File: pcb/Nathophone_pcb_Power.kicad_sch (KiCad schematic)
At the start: 54 parts, among them J1 PJ-063AH, J12 54202-S0806ALF, Q1 2N7002H, Q2 2N7002H, Q3 FDN340P, Q4 FQD11P06TM, Q5 FDN340P, SW1 1-1571986-1, U1 LT8650SEV_PBF, U2 SPX3819M5-L-3-3

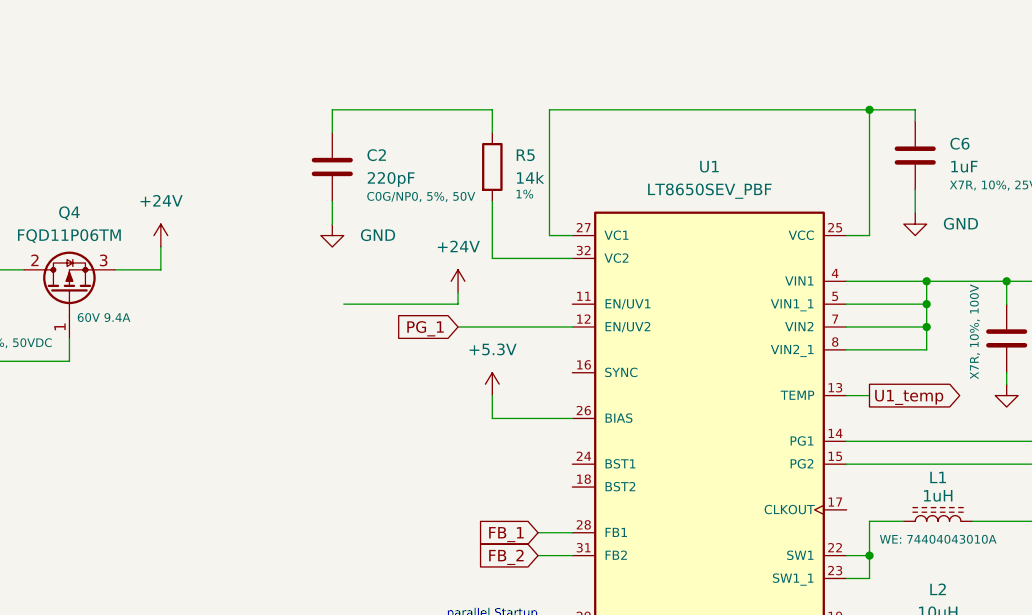
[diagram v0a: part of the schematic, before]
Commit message: ADDED Grounding Structure
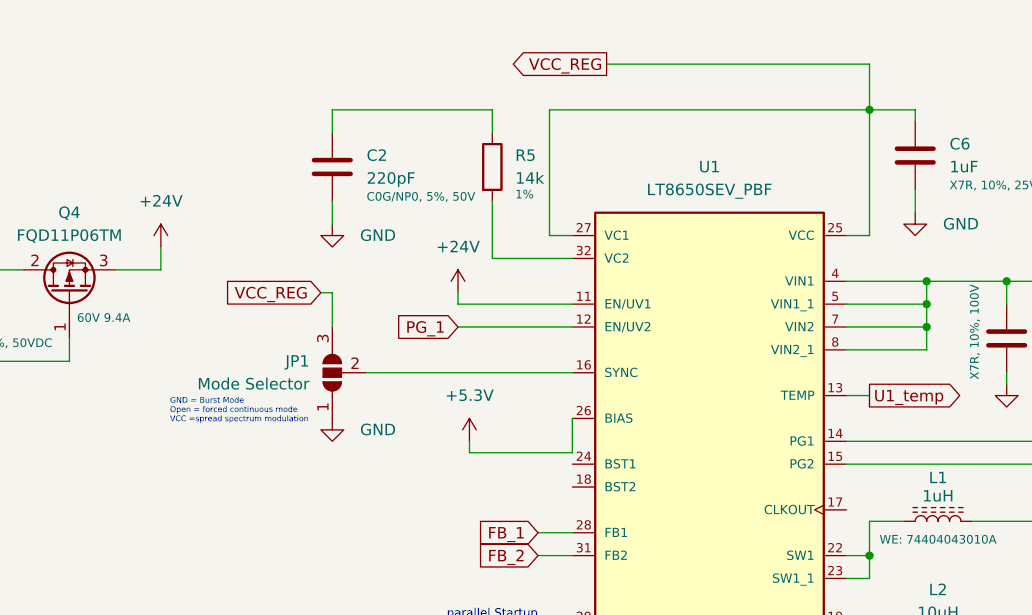
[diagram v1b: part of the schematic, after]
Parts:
- added JP1: Mode Selector, Jumper:SolderJumper-3_P1.3mm_Open_RoundedPad1.0x1.5mm, symbol Jumper:SolderJumper_3_Open
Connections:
- net +24V: now also U1.11 (EN/UV1)
- net GND: now also JP1.1 (A)
- net VCC_REG: now reaches C6.1, U1.25 (VCC), U1.27 (VC1)
- net VCC_REG: now also JP1.3 (B)
- net at U1.16 (SYNC): now also JP1.2 (C)
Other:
- note added: "GND = Burst Mode Open = forced continuous mode VCC =spread spectrum modulation"

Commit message: FINISHED Version 1, Checked heights
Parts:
- added F5, F6, F7: Polyfuse, Fuse:Fuse_1206_3216Metric, symbol Device:Polyfuse
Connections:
- net +24V: now also F6.1; no longer J12.2 (Pin_2)
- net +3.3V_int: now also F7.1; no longer J12.6 (Pin_6)
- net +5.3V: now also F5.1; no longer J12.4 (Pin_4)
- new net: F5.2, J12.4 (Pin_4)
- new net: F6.2, J12.2 (Pin_2)
- new net: F7.2, J12.6 (Pin_6)

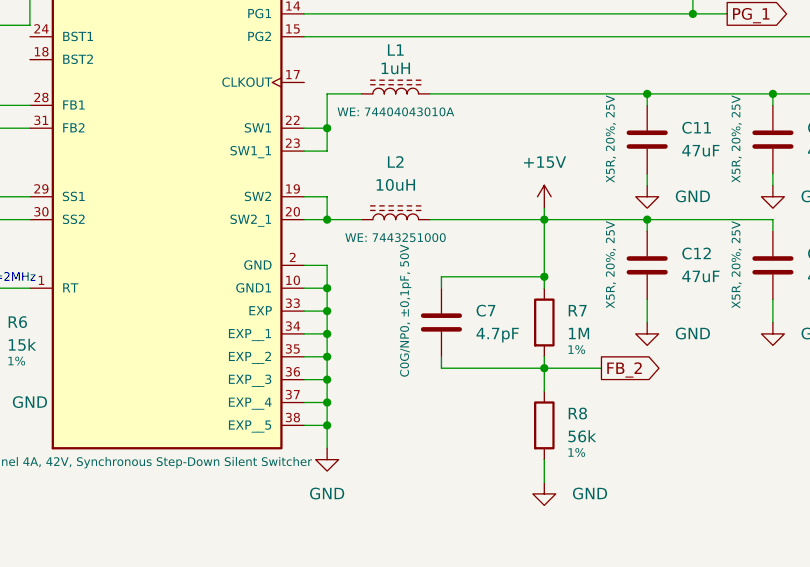
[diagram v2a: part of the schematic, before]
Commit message: CHANGED small things, removed tiny 0201 cap
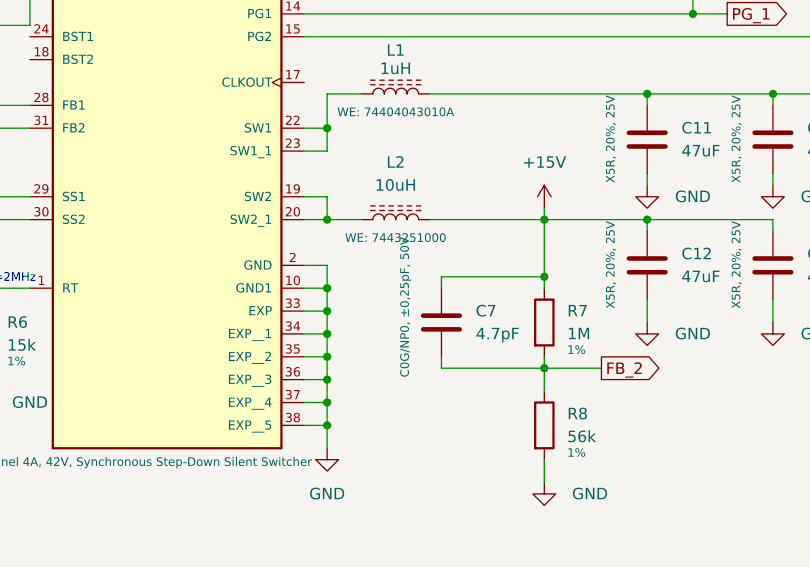
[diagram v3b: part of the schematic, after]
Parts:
- C1: MPN (none) -> ECH-U1H103JX5
- C10, C5: MPN (none) -> CL21C103JBF1PNE
- C11, C12, C14, C15: MPN (none) -> C3216X5R1E476M160AC
- C13, C16: MPN (none) -> CL31B106KAHNNNE
- C17, C2: MPN (none) -> CL21C221JBANNNC
- C3, C4: MPN (none) -> CL21C102JBCNFNC
- C6: MPN (none) -> CL21B105KAFNNNE
- C7: footprint Capacitor_SMD:C_0201_0603Metric_Pad0.64x0.40mm_HandSolder -> Capacitor_SMD:C_0402_1005Metric; DigiKey_PartNo 1276-1792-2-ND -> 1276-6694-2-ND; Key Info C0G/NP0, ±0,1pF, 50V -> C0G/NP0, ±0,25pF, 50V; MPN (none) -> CL05C4R7CB51PNC
- C8, C9: MPN (none) -> C3216X7R2A475K160AC
- C93: MPN (none) -> GXC1H470MCQ1GS
- D1, D11: MPN (none) -> CMD15-21VGD/TR8
- D2: MPN (none) -> TPSMB2616CA
- F5, F6, F7: MPN (none) -> 0ZCJ0025AF2E
- J1: MPN (none) -> PJ-063AH
- J12: MPN (none) -> 54202-S0806ALF
- L1: MPN (none) -> 74404043010A
- L2: MPN (none) -> 7443251000
- Q1, Q2: MPN (none) -> 2N7002H-7
- Q3, Q5: MPN (none) -> FDN340P
- Q4: MPN (none) -> FQD11P06TM
- R1: MPN (none) -> CRCW0805750RFKEA
- R10, R9: MPN (none) -> CRCW0805100KFKEA
- R11, R2, R3, R4, R7: MPN (none) -> CRCW08051M00FKEA
- R44: MPN (none) -> CRCW08053K60FKEA
- R46: MPN (none) -> MFHA1206R5000FC
- R48: MPN (none) -> CRCW0805178KFKEA
- R5: MPN (none) -> CRCW080514K0FKEA
- R6: MPN (none) -> CRCW080515K0FKEA
- R8: MPN (none) -> CRCW080556K0FKEA
- SW1: MPN (none) -> 1-1571986-1
- U1: MPN (none) -> LT8650SEV#PBF
- U2: MPN (none) -> SPX3819M5-L-3-3/TR

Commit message: SIMULATED Transmission line, LAST checks, ORDERED pcb
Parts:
- renumbered C93 to C13, C13 to C14, C14 to C15, C15 to C16, C16 to C17, C17 to C18, D11 to D3, F6 to F1, F5 to F2, F7 to F3, J12 to J2, R9 to R10, R46 to R11, R10 to R12, R11 to R13, R48 to R14, R44 to R3, R3 to R4, R4 to R5, R5 to R6, R6 to R7, R7 to R8, R8 to R9, TP6 to TP1

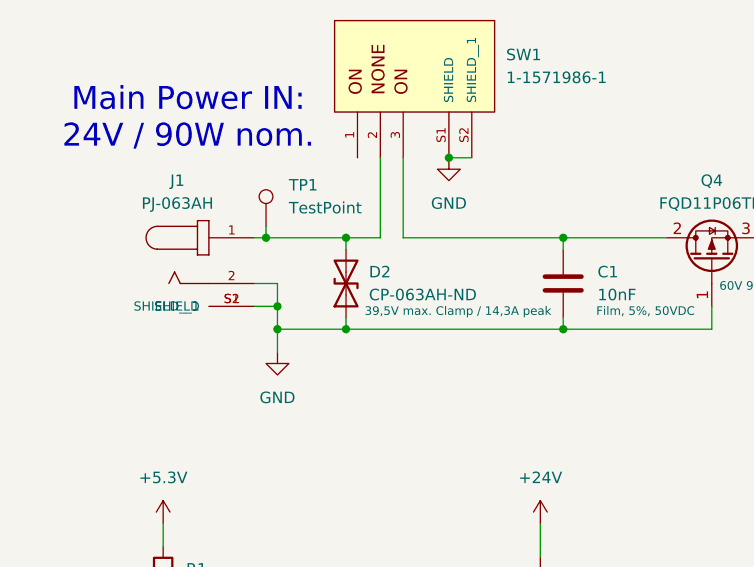
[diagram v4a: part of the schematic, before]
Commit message: CORRECTED TVS Diode polarisation
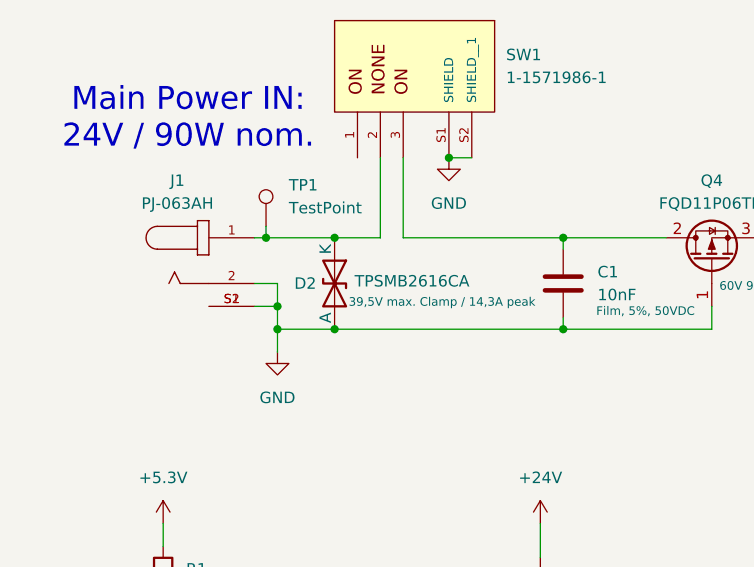
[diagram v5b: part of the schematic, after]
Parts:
- D2: value CP-063AH-ND -> TPSMB2616CA
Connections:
- net GND: now also D2.2 (A); no longer D2.1 (A1)
- net at J1.1, SW1.2, TP1.1: now also D2.1 (K); no longer D2.2 (A2)
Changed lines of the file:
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@@
 	)
 	(junction
+		(at 46.99 45.72)
+		(diameter 0)
+		(color 0 0 0 0)
+	)
+	(junction
 		(at 255.27 81.28)
 		(diameter 0)
@@
 	)
 	(junction
+		(at 46.99 55.88)
+		(diameter 0)
+		(color 0 0 0 0)
+	)
+	(junction
 		(at 184.15 49.53)
 		(diameter 0)
@@
 	)
 	(junction
-		(at 48.26 55.88)
-		(diameter 0)
-		(color 0 0 0 0)
-	)
-	(junction
 		(at 171.45 135.89)
 		(diameter 0)
@@
 	)
 	(junction
-		(at 48.26 45.72)
-		(diameter 0)
-		(color 0 0 0 0)
-	)
-	(junction
 		(at 95.25 156.21)
 		(diameter 0)
@@
 	(wire
 		(pts
-			(xy 48.26 55.88) (xy 72.39 55.88)
-		)
-		(stroke
-			(width 0)
-			(type default)
-		)
-	)
-	(wire
-		(pts
 			(xy 175.26 105.41) (xy 177.8 105.41)
 		)
@@
 	(wire
 		(pts
-			(xy 48.26 45.72) (xy 48.26 46.99)
-		)
-		(stroke
-			(width 0)
-			(type default)
-		)
-	)
-	(wire
-		(pts
 			(xy 201.93 87.63) (xy 201.93 93.98)
 		)
@@
 	(wire
 		(pts
-			(xy 40.64 55.88) (xy 48.26 55.88)
+			(xy 40.64 55.88) (xy 46.99 55.88)
 		)
 		(stroke
@@
 	(wire
 		(pts
+			(xy 46.99 55.88) (xy 72.39 55.88)
+		)
+		(stroke
+			(width 0)
+			(type default)
+		)
+	)
+	(wire
+		(pts
 			(xy 40.64 53.34) (xy 40.64 55.88)
 		)
@@
 	(wire
 		(pts
-			(xy 48.26 45.72) (xy 52.07 45.72)
-		)
-		(stroke
-			(width 0)
-			(type default)
-		)
-	)
-	(wire
-		(pts
 			(xy 175.26 59.69) (xy 177.8 59.69)
 		)
@@
 	(wire
 		(pts
-			(xy 39.37 45.72) (xy 48.26 45.72)
+			(xy 39.37 45.72) (xy 46.99 45.72)
 		)
 		(stroke
@@
 	(wire
 		(pts
-			(xy 48.26 54.61) (xy 48.26 55.88)
-		)
-		(stroke
-			(width 0)
-			(type default)
-		)
-	)
-	(wire
-		(pts
 			(xy 238.76 135.89) (xy 238.76 137.16)
 		)
@@
 	(wire
 		(pts
+			(xy 46.99 45.72) (xy 52.07 45.72)
+		)
+		(stroke
+			(width 0)
+			(type default)
+		)
+	)
+	(wire
+		(pts
 			(xy 210.82 149.86) (xy 210.82 152.4)
 		)
@@
 	(symbol
 		(lib_id "Device:D_TVS")
-		(at 48.26 50.8 90)
+		(at 46.99 50.8 270)
 		(unit 1)
 		(exclude_from_sim no)
@@
 		(dnp no)
 		(property "Reference" "D2"
-			(at 50.8 49.5299 90)
+			(at 44.958 50.8 90)
 			(effects
 				(font
@@
 			)
 		)
-		(property "Value" "CP-063AH-ND"
-			(at 50.8 52.0699 90)
+		(property "Value" "TPSMB2616CA"
+			(at 61.976 50.546 90)
 			(effects
 				(font
@@
 		)
 		(property "Footprint" "Diode_SMD:D_SMB"
-			(at 48.26 50.8 0)
+			(at 46.99 50.8 0)
 			(effects
 				(font
@@
 		)
 		(property "Datasheet" "https://www.littelfuse.com/assetdocs/tvs-diode-tpsmb-datasheet?assetguid=E7A196A8-A225-4724-AB76-7C22E0D48557"
-			(at 48.26 50.8 0)
+			(at 46.99 50.8 0)
 			(effects
 				(font
@@
 		)
 		(property "Description" "Bidirectional transient-voltage-suppression diode"
-			(at 48.26 50.8 0)
+			(at 46.99 50.8 0)
 			(effects
 				(font
@@
 		)
 		(property "DigiKey_PartNo" "18-TPSMB2616CATR-ND"
-			(at 48.26 50.8 90)
+			(at 46.99 50.8 90)
 			(effects
 				(font
@@
 		)
 		(property "Key Info" "39,5V max. Clamp / 14,3A peak"
-			(at 60.706 53.848 90)
+			(at 58.928 52.832 90)
 			(effects
 				(font
@@
 		)
 		(property "MPN" "TPSMB2616CA"
-			(at 48.26 50.8 90)
+			(at 46.99 50.8 90)
 			(effects
 				(font
